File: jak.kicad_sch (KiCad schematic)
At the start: 92 parts, among them SW1 SW_Push, SW10 SW_Push, SW10_r1 SW_Push, SW11 SW_Push, SW11_r1 SW_Push, SW12 SW_Push, SW12_r1 SW_Push, SW13 SW_Push, SW13_r1 SW_Push, SW14 SW_Push, SW14_r1 SW_Push, SW15 SW_Push, SW15_r1 SW_Push, SW16 SW_Push, SW16_r1 SW_Push, SW17 SW_Push, SW17_r1 SW_Push, SW18 SW_Push, SW18_r1 SW_Push, SW1_r1 SW_Push, SW2 SW_Push, SW2_r1 SW_Push, SW3 SW_Push, SW3_r1 SW_Push, SW4 SW_Push, SW4_r1 SW_Push, SW5 SW_Push, SW5_r1 SW_Push, SW6 SW_Push, SW6_r1 SW_Push, SW7 SW_Push, SW7_r1 SW_Push, SW8 SW_Push, SW8_r1 SW_Push, SW9 SW_Push, SW9_r1 SW_Push

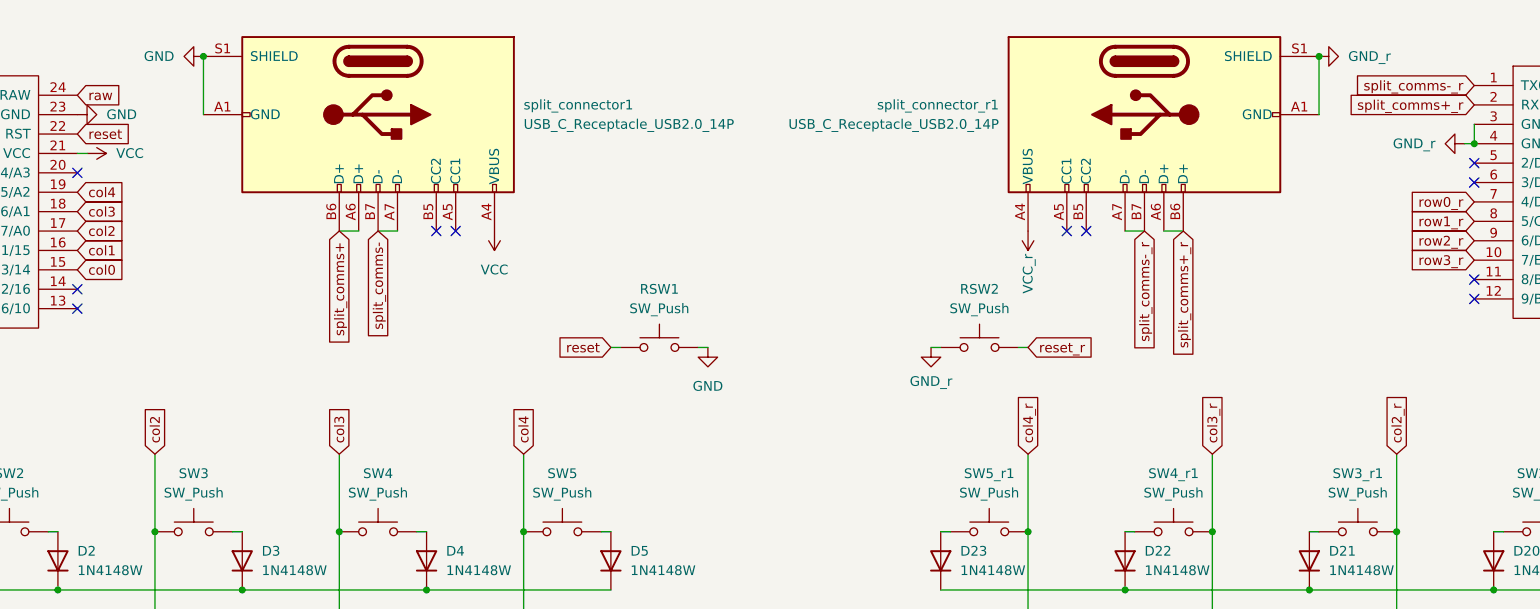
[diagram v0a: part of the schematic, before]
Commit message: Replaced the through-hole surface USB-C connector with a flush one
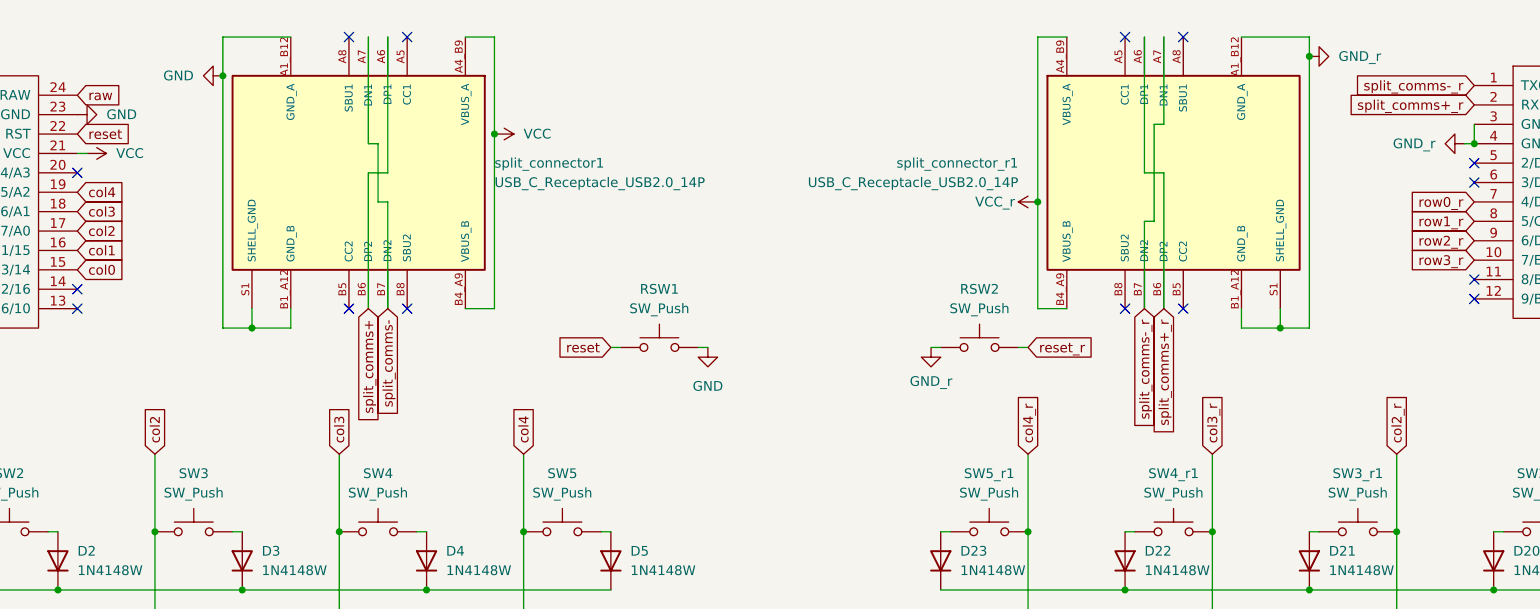
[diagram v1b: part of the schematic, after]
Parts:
- split_connector1, split_connector_r1: footprint Connector_USB:USB_C_Receptacle_GCT_USB4105-xx-A_16P_TopMnt_Horizontal -> USB4505-03-0-A_REVA:GCT_USB4505-03-0-A_REVA; symbol Connector:USB_C_Receptacle_USB2.0_14P -> USB4505-03-0-A_REVA:USB4505-03-0-A_REVA; Availability (none) -> In Stock; Check_prices (none) -> https://www.snapeda.com/parts/USB4505-03-0-A/Global+Connect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; Description_1 (none) -> USB-C (USB TYPE-C) USB 2.0 Receptacle Connector 24 (16+8 Du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; MANUFACTURER (none) -> GCT; MAXIMUM_PACKAGE_HEIGHT (none) -> 2.46mm; MF (none) -> Global Connector Technology; MP (none) -> USB4505-03-0-A; PARTREV (none) -> A; Package (none) -> None; Price (none) -> None; Purchase-URL (none) -> https://www.snapeda.com/api/url_track_click_mouser/?unipart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; STANDARD (none) -> Manufacturer Recommendations; SnapEDA_Link (none) -> https://www.snapeda.com/parts/USB4505-03-0-A/Global+Connect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
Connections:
- net GND: now also split_connector1.A1_B12 (GND_A), split_connector1.B1_A12 (GND_B), split_connector1.S2 (SHELL_GND), split_connector1.S3 (SHELL_GND), split_connector1.S4 (SHELL_GND); no longer split_connector1.A1 (GND), split_connector1.A12 (GND), split_connector1.B1 (GND), split_connector1.B12 (GND)
- net GND_r: now also split_connector_r1.A1_B12 (GND_A), split_connector_r1.B1_A12 (GND_B), split_connector_r1.S2 (SHELL_GND), split_connector_r1.S3 (SHELL_GND), split_connector_r1.S4 (SHELL_GND); no longer split_connector_r1.A1 (GND), split_connector_r1.A12 (GND), split_connector_r1.B1 (GND), split_connector_r1.B12 (GND)
- net VCC: now also split_connector1.A4_B9 (VBUS_A), split_connector1.B4_A9 (VBUS_B); no longer split_connector1.A4 (VBUS), split_connector1.A9 (VBUS), split_connector1.B4 (VBUS), split_connector1.B9 (VBUS)
- net VCC_r: now also split_connector_r1.A4_B9 (VBUS_A), split_connector_r1.B4_A9 (VBUS_B); no longer split_connector_r1.A4 (VBUS), split_connector_r1.A9 (VBUS), split_connector_r1.B4 (VBUS), split_connector_r1.B9 (VBUS)
- no-connect marks 20 -> 24
